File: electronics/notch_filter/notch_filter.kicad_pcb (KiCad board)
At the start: 2 copper layers, 42.4 x 46.2 mm, 32 parts, among them J1 Conn_01x03, J2 Conn_01x03, J3 Output, J4 In, J5 module_2x15_left_input, J6 module_2x15_right_input, U1 opamp_single_8pin

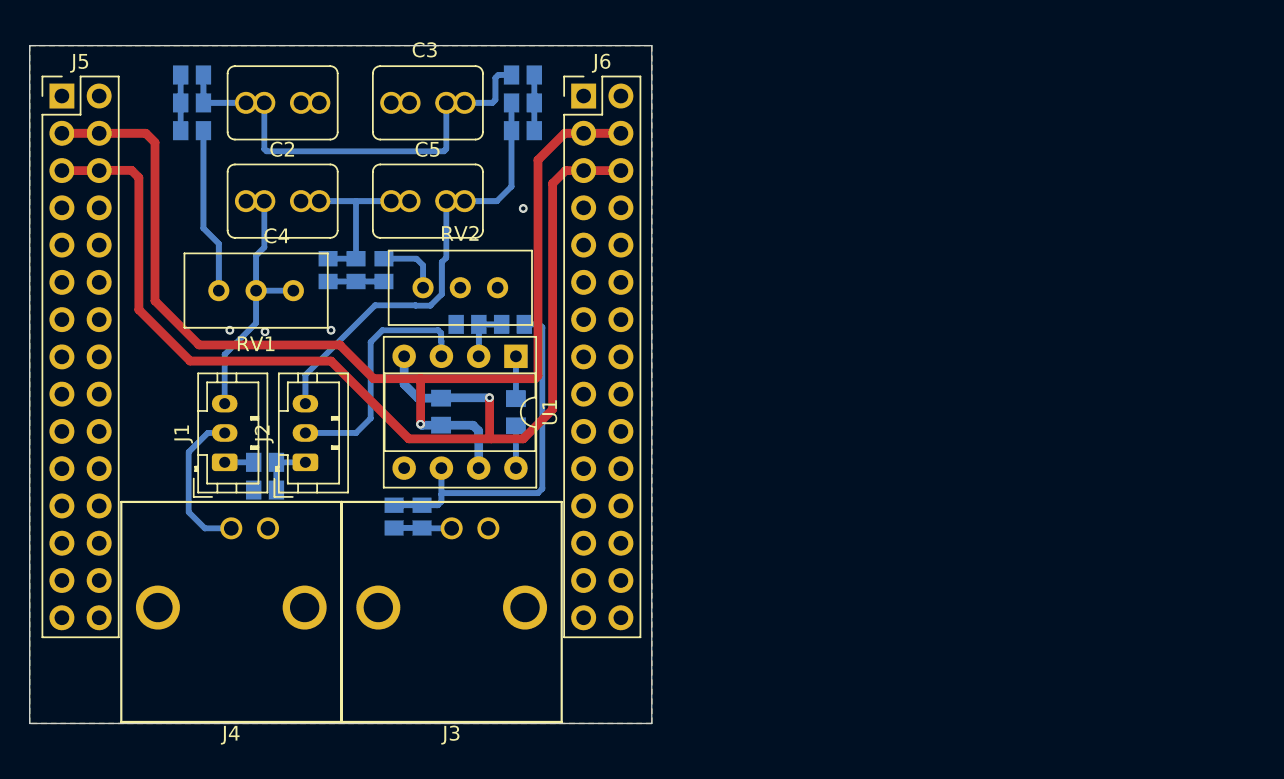
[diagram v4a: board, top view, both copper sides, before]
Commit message: footprint changes, changed power rails, silk placed, added labels, increased size of labels
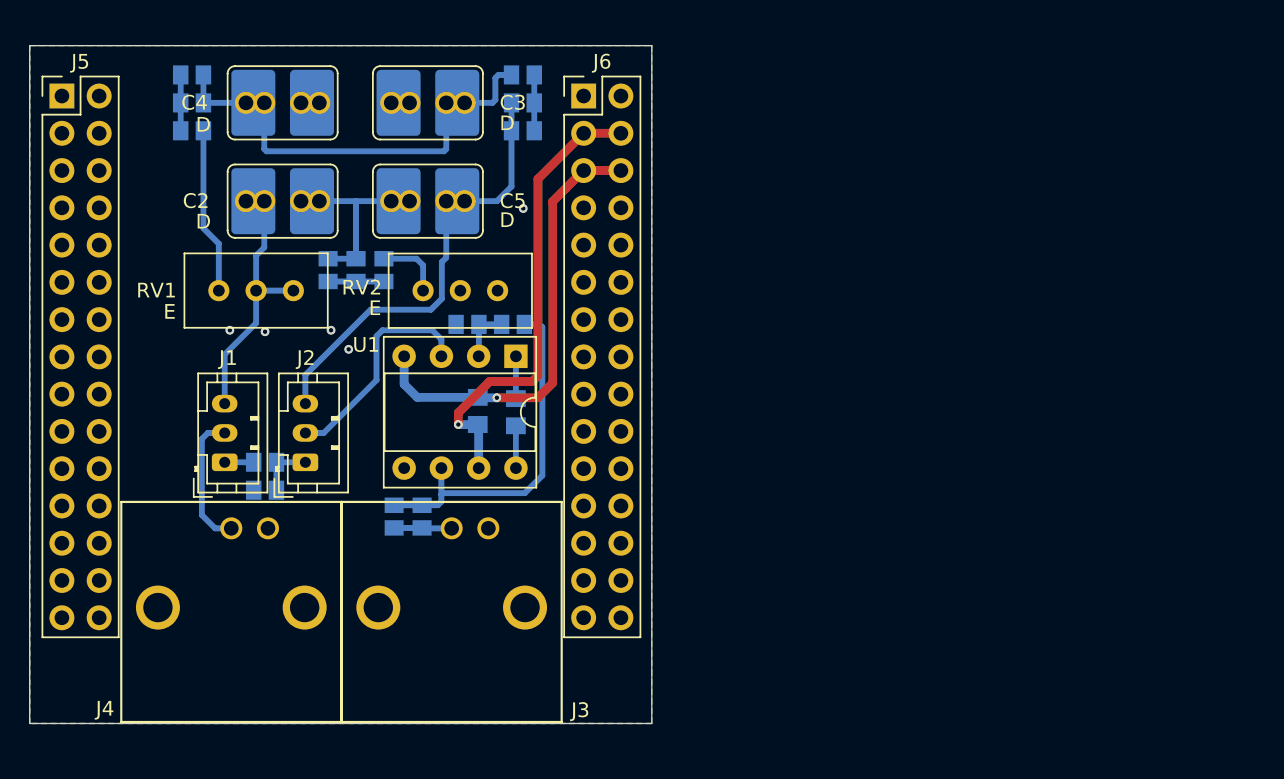
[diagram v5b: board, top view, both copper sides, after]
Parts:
- added N3: A:, SquantorLabels:Label_Note_medium, B.Cu at (75.6, 81.6)
- added N4: B:, SquantorLabels:Label_Note_medium, B.Cu at (75.6, 87.2)
- added N5: C:, SquantorLabels:Label_Note_medium, B.Cu at (75.6, 90.6)
- added N6: D:, SquantorLabels:Label_Note_medium, B.Cu at (90.6, 81.7)
- added N7: E:, SquantorLabels:Label_Note_medium, B.Cu at (90.6, 87.3)
- added N8: Hz:, SquantorLabels:Label_Note_medium, B.Cu at (90.6, 90.7)
- C2, C3, C4, C5: footprint SquantorRcl:C-025_050-050X100-film -> SquantorRcl:C-025_050-050X100-0805-3516-film
- C6: value compen -> comp
- N1: value 20230414 -> 20230420
- R1: value 10K -> 100
- moved N2 29.6 mm to (68.8, 56.2), turned to 180 degrees
- moved N1 21.7 mm to (69.4, 60.1), turned to 180 degrees
- moved C1 2.50 mm to (89.3, 71.0)
- moved RV2 0.20 mm to (90.7, 62.8)
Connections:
- J5 pad 13: unconnected-(J5-Pad13) -> GND
- J5 pad 15: unconnected-(J5-Pad15) -> GND
- J5 pad 3: +15V -> unconnected-(J5-Pad3)
- J5 pad 4: +15V -> unconnected-(J5-Pad4)
- J5 pad 5: -15V -> unconnected-(J5-Pad5)
- J5 pad 6: -15V -> unconnected-(J5-Pad6)
- J6 pad 14: unconnected-(J6-Pad14) -> GND
- J6 pad 16: unconnected-(J6-Pad16) -> GND
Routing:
- net -15V: track 78.5 -> 30.7 mm
- net +15V: track 76.7 -> 31.9 mm
- net Net-(J2-Pad2): track 16.9 -> 15.3 mm
- net Net-(J1-Pad2): track 10.4 -> 9.29 mm
- net Net-(R2-Pad2): track 25.0 -> 24.4 mm
- net GND: vias 4 -> 5

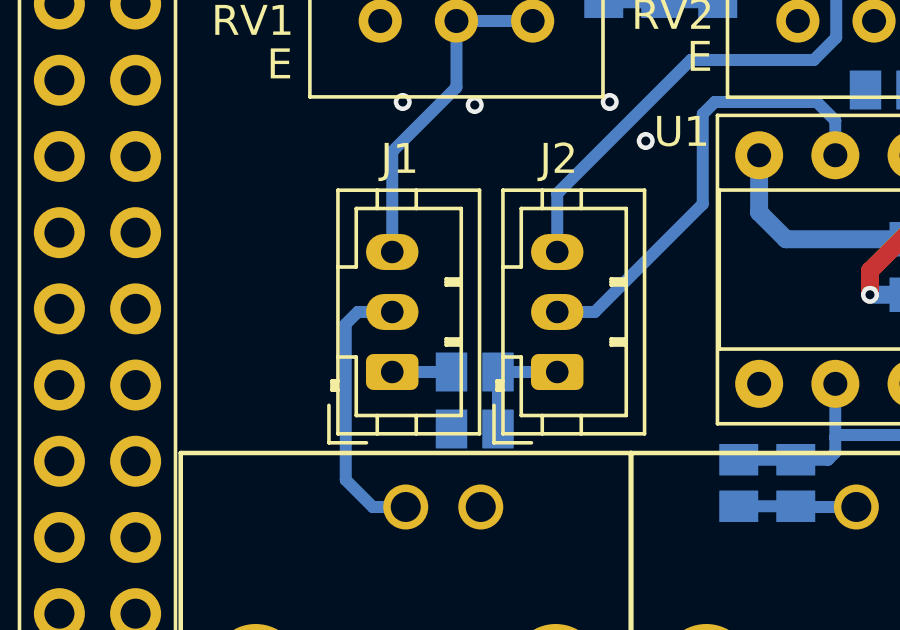
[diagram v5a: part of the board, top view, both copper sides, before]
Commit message: added 1M input resistor
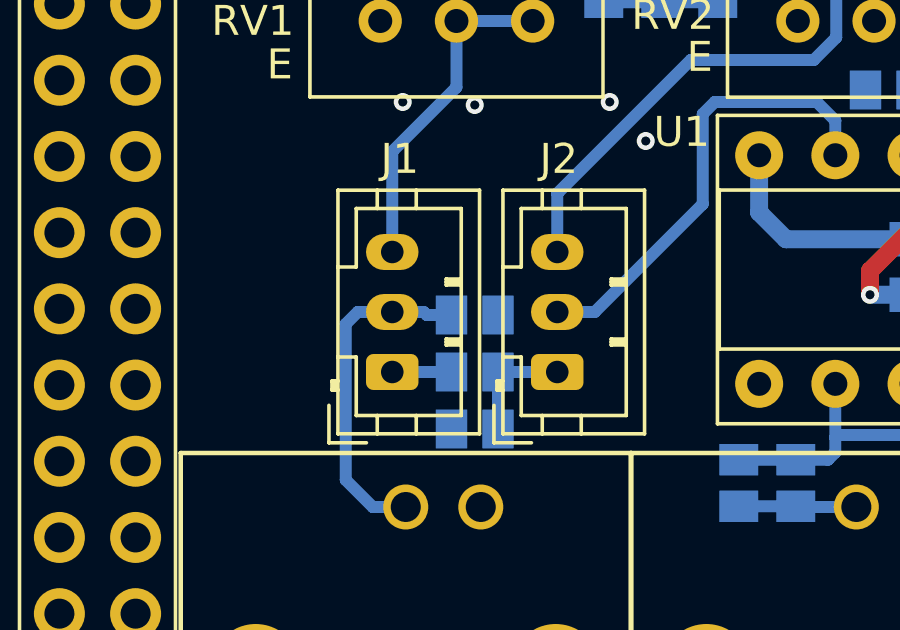
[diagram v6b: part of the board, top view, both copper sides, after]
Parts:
- added R16: 1M, SquantorRcl:R_0805+0603, B.Cu at (74.8, 72.6)
- N1: value 20230420 -> 20230421
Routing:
- net Net-(J1-Pad2): track 9.29 -> 11.3 mm
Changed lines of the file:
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@@
       (effects (font (size 1 1) (thickness 0.15)) (justify mirror))
     )
-    (fp_text value "20230420" (at 0.8 0.1) (layer "B.SilkS")
+    (fp_text value "20230421" (at 0.8 0.1) (layer "B.SilkS")
       (effects (font (size 0.8 0.8) (thickness 0.15)) (justify mirror))
     )
@@
     )
   )
+  (footprint "SquantorRcl:R_0805+0603" (layer "B.Cu")
+    (at 74.8 72.6 180)
+    (descr "Resistor SMD 0805, reflow soldering, Vishay (see dcrcw.pdf)")
+    (tags "resistor 0805")
+    (property "Sheetfile" "notch_filter.kicad_sch")
+    (property "Sheetname" "")
+    (attr smd)
+    (fp_text reference "R16" (at 0 1.5) (layer "B.SilkS")
+      (effects (font (size 1 1) (thickness 0.15)) (justify mirror))
+    )
+    (fp_text value "1M" (at 0 2.9) (layer "B.SilkS")
+      (effects (font (size 1 1) (thickness 0.15)) (justify mirror))
+    )
+    (fp_poly (pts
+        (xy -0.1 0.6)
+        (xy -0.1 -0.6)
+        (xy 0.1 -0.6)
+        (xy 0.1 0.6)
+      ) (layer "B.SilkS") (width 0.1) (fill solid))
+    (fp_line (start 1.55 0.95) (end 1.55 -0.95) (layer "B.CrtYd") (width 0.05))
+    (fp_line (start -1.55 0.95) (end -1.55 -0.95) (layer "B.CrtYd") (width 0.05))
+    (fp_line (start -1.55 0.95) (end 1.55 0.95) (layer "B.CrtYd") (width 0.05))
+    (fp_line (start -1.55 -0.95) (end 1.55 -0.95) (layer "B.CrtYd") (width 0.05))
+    (fp_line (start -1 -0.625) (end -1 0.625) (layer "B.Fab") (width 0.1))
+    (fp_line (start 1 0.625) (end 1 -0.625) (layer "B.Fab") (width 0.1))
+    (fp_line (start -1 0.625) (end 1 0.625) (layer "B.Fab") (width 0.1))
+    (fp_line (start 1 -0.625) (end -1 -0.625) (layer "B.Fab") (width 0.1))
+    (pad "1" smd rect (at -0.775 0 180) (size 1.05 1.3) (layers "B.Cu" "B.Paste" "B.Mask")
+      (net 2 "GND") (pintype "passive"))
+    (pad "2" smd rect (at 0.775 0 180) (size 1.05 1.3) (layers "B.Cu" "B.Paste" "B.Mask")
+      (net 40 "Net-(J1-Pad2)") (pintype "passive"))
+    (model "${KICAD6_3DMODEL_DIR}/Resistor_SMD.3dshapes/R_0805_2012Metric.step"
+      (offset (xyz 0 0 0))
+      (scale (xyz 1 1 1))
+      (rotate (xyz 0 0 0))
+    )
+  )
   (footprint "SquantorLabels:Label_Note_medium" (layer "B.Cu")
     (at 90.6 81.7 180)
@@
   (segment (start 70.9 72.5) (end 72.05 72.5) (width 0.4) (layer "B.Cu") (net 40))
   (segment (start 72.5 79) (end 71.4 79) (width 0.4) (layer "B.Cu") (net 40))
+  (segment (start 73.1 72.5) (end 73.2 72.6) (width 0.4) (layer "B.Cu") (net 40))
+  (segment (start 73.2 72.6) (end 74.025 72.6) (width 0.4) (layer "B.Cu") (net 40))
   (segment (start 70.5 72.9) (end 70.9 72.5) (width 0.4) (layer "B.Cu") (net 40))
   (segment (start 70.5 78.1) (end 70.5 72.9) (width 0.4) (layer "B.Cu") (net 40))
+  (segment (start 72.05 72.5) (end 73.1 72.5) (width 0.4) (layer "B.Cu") (net 40))
   (segment (start 78.8 72.5) (end 82.4 68.9) (width 0.4) (layer "B.Cu") (net 41))
   (segment (start 82.4 65.9) (end 82.8 65.5) (width 0.4) (layer "B.Cu") (net 41))

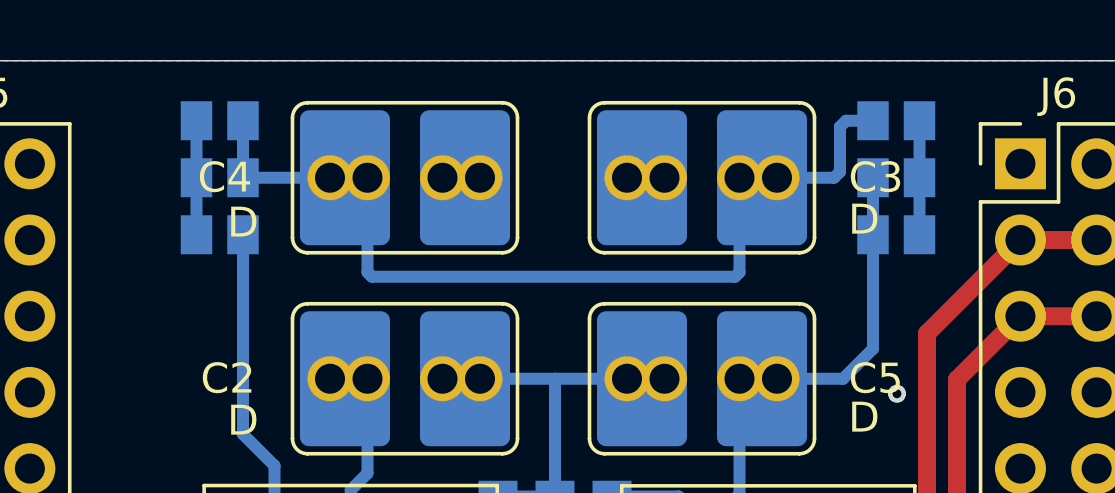
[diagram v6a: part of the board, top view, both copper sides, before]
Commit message: ERC/DRC passes, small ergonomic changes
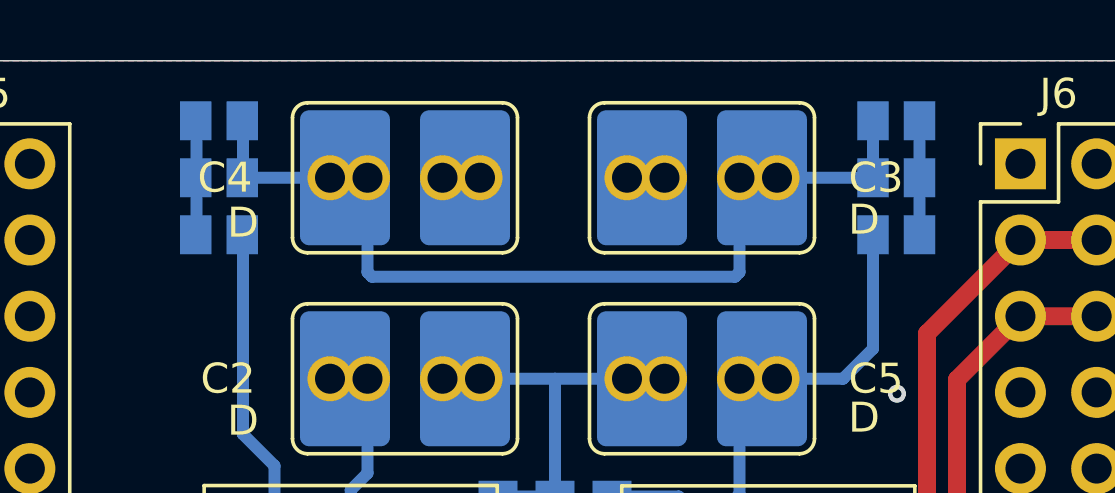
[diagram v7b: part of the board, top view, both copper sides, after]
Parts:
- N1: value 20230421 -> 20230507
- moved R10 3.80 mm to (92.4, 51.9), turned to 180 degrees
- moved R15 3.80 mm to (92.4, 48.1), turned to 0 degrees
- moved R13 1.90 mm to (69.8, 48.1)
- moved R8 1.90 mm to (69.8, 50.0)
- turned R11 to 0 degrees
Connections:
- R10 pad 1: Net-(C3-Pad2) -> Net-(R11-Pad2)
- R10 pad 2: Net-(R10-Pad2) -> /FILT_OUT
- R11 pad 1: Net-(R10-Pad2) -> Net-(C3-Pad2)
- R11 pad 2: /FILT_OUT -> Net-(R11-Pad2)
- R15 pad 1: Net-(R10-Pad2) -> Net-(C3-Pad2)
- R15 pad 2: /FILT_OUT -> Net-(R11-Pad2)
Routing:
- net Net-(R11-Pad2): track 0.00 -> 3.80 mm
- net Net-(R10-Pad2): track 3.80 -> 0.00 mm
- net /FILT_OUT: track 29.5 -> 27.6 mm

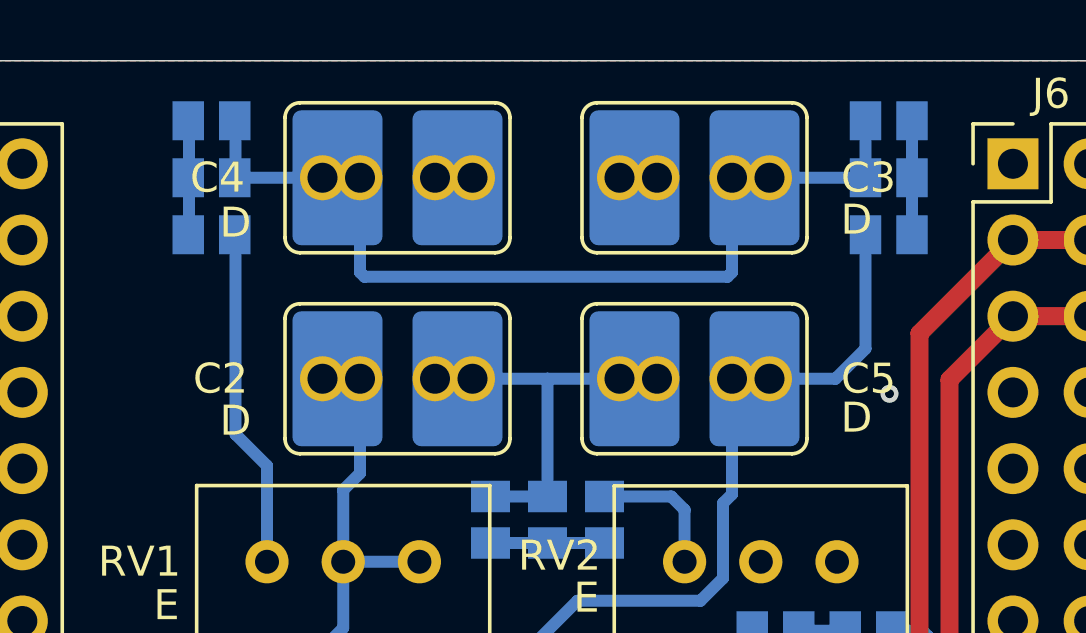
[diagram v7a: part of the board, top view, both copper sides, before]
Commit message: updated notch filter
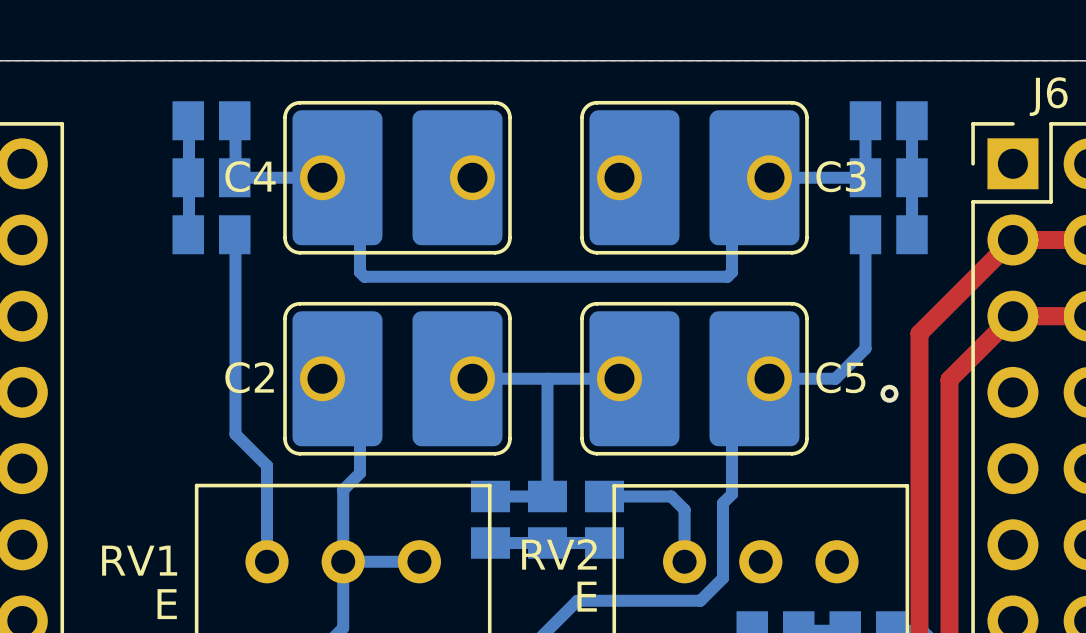
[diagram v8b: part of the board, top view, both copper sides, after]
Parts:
- C2, C3, C4, C5: footprint SquantorRcl:C-025_050-050X100-0805-3516-film -> SquantorRcl:C-050-050X100-0805-3516-film
- N1: value 20230507 -> 20230530
